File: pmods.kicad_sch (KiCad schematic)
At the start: 28 parts, among them J10 Conn_02x06_Odd_Even, J11 Conn_02x06_Odd_Even, J12 Conn_02x06_Odd_Even, J5 Conn_02x06_Odd_Even, J6 Conn_02x06_Odd_Even, J7 Conn_02x06_Odd_Even, J8 Conn_02x06_Odd_Even, J9 Conn_02x06_Odd_Even, SW1 SW_DIP_x08, SW2 SW_Push, SW3 SW_Push, SW4 SW_Push, SW5 SW_Push, SW6 SW_Push, SW7 SW_Push, SW8 SW_Push, SW9 SW_Push

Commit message: Adicionando novos datasheets e comecando power
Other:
- title: ECP5 85F Platonic Board -> PatchLogic 85 FPGA Board
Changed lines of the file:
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@@
 	(paper "A4")
 	(title_block
-		(title "ECP5 85F Platonic Board")
+		(title "PatchLogic 85 FPGA Board")
 		(rev "V0.1")
 		(company "ODHIN Unicamp")

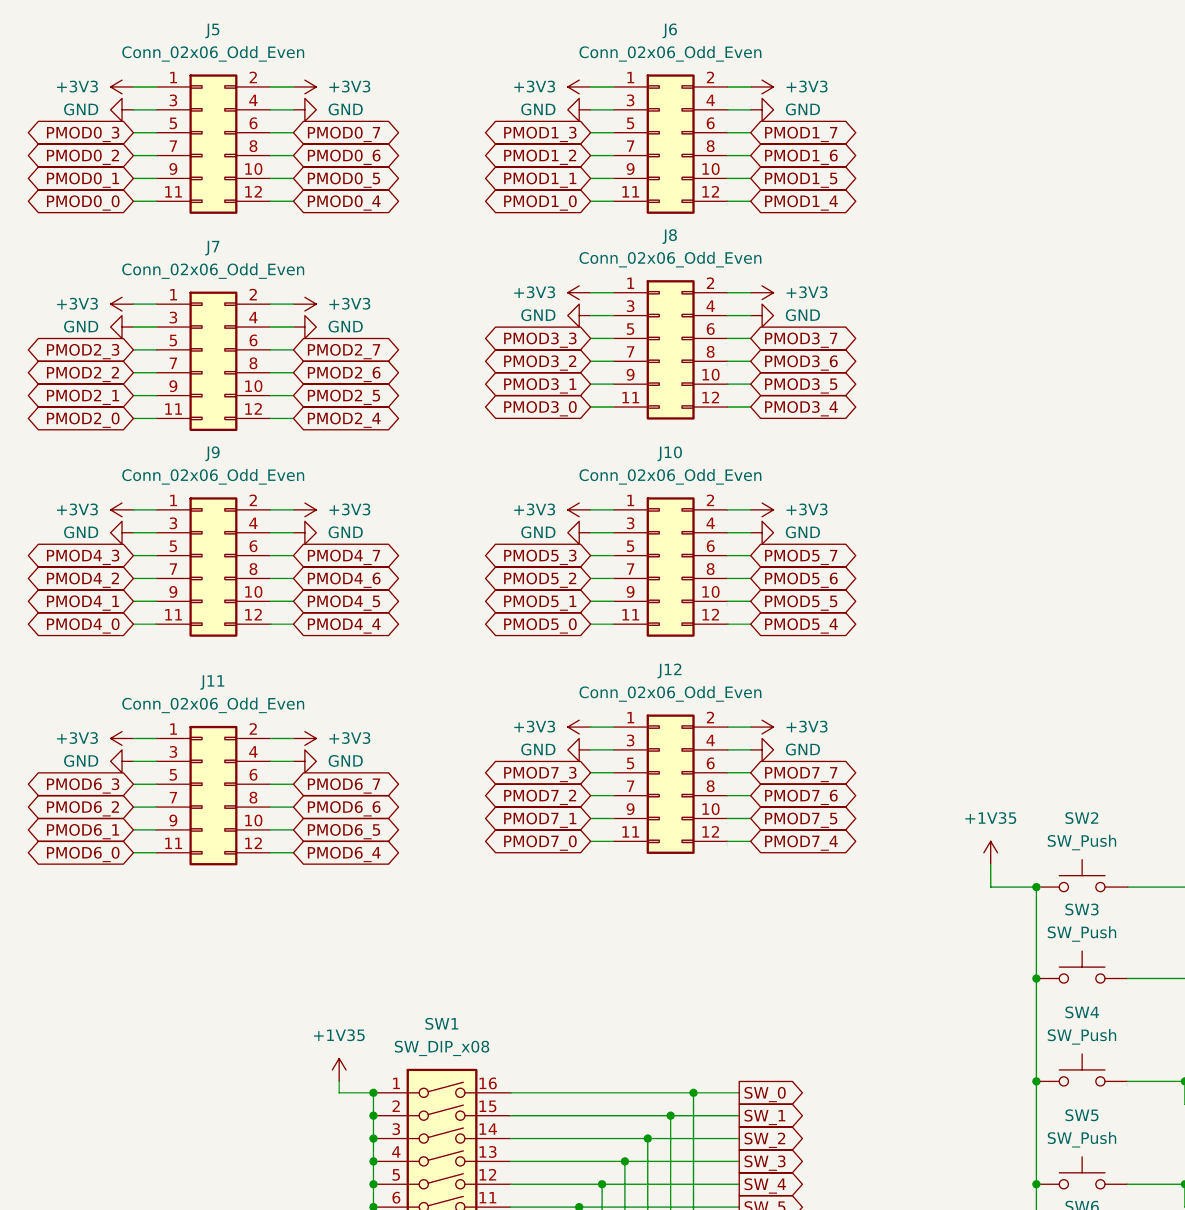
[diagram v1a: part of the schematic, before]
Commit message: Implementando power e ligando jtag e flash a fpga
Implementando circuito de power. Ligando JTAG e memoria FLASH quad SPI a
FPGA. Iniciando implementacão da DRAM e outros modulos
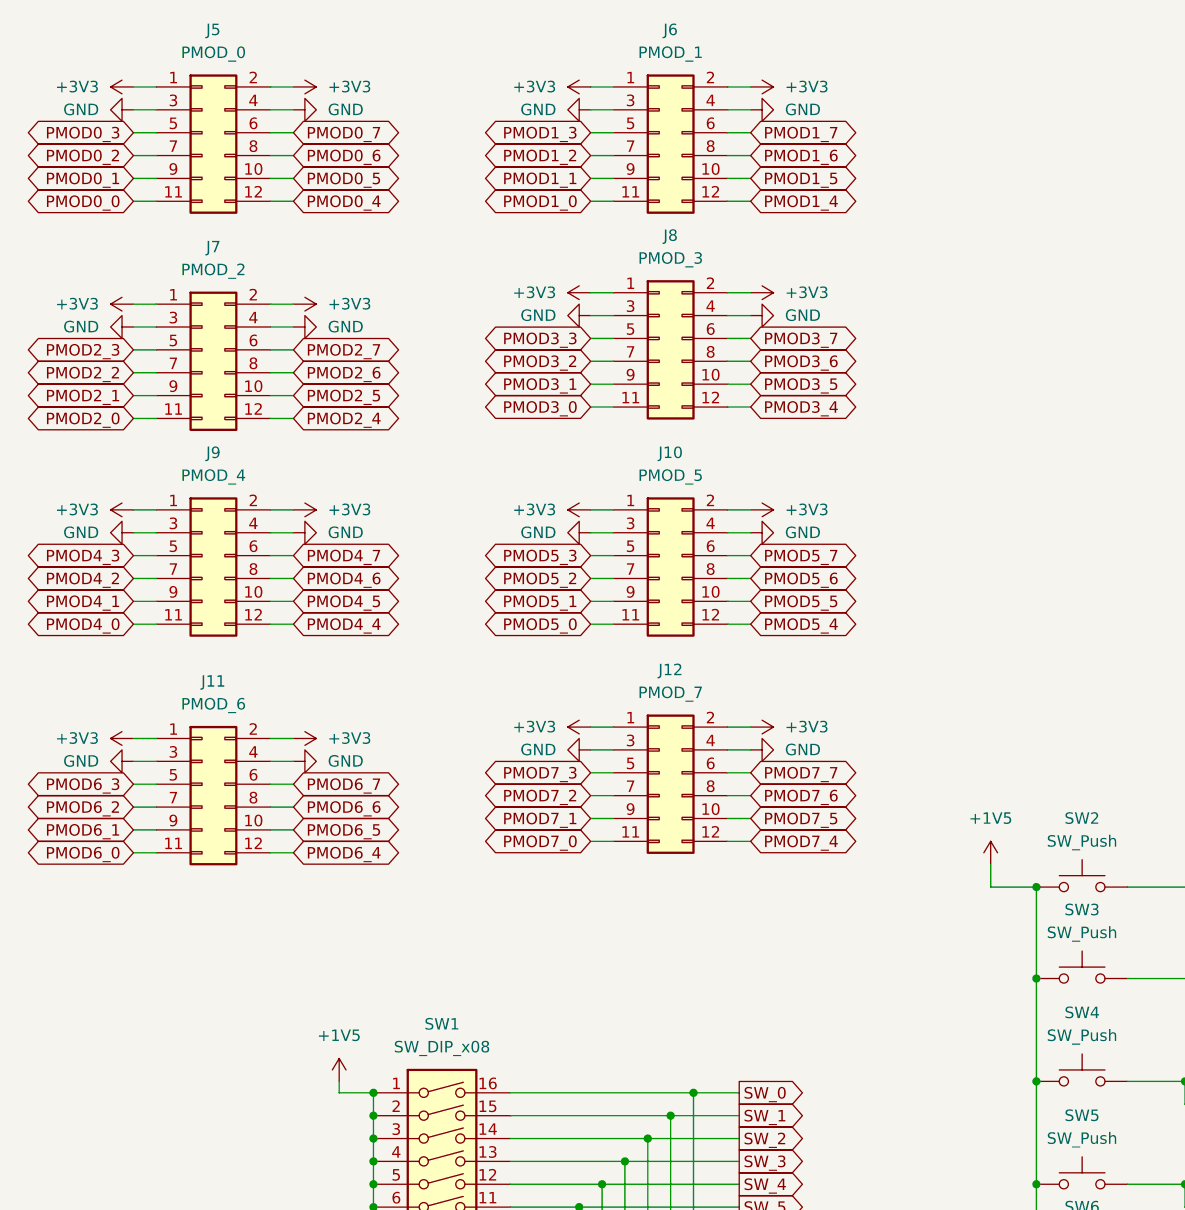
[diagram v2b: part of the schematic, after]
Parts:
- J10: value Conn_02x06_Odd_Even -> PMOD_5
- J11: value Conn_02x06_Odd_Even -> PMOD_6
- J12: value Conn_02x06_Odd_Even -> PMOD_7
- J5: value Conn_02x06_Odd_Even -> PMOD_0
- J6: value Conn_02x06_Odd_Even -> PMOD_1
- J7: value Conn_02x06_Odd_Even -> PMOD_2
- J8: value Conn_02x06_Odd_Even -> PMOD_3
- J9: value Conn_02x06_Odd_Even -> PMOD_4
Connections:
- net +1V35 renamed +1V5
